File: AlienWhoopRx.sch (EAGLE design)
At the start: 16 parts, among them U1 XN297L, Y1 16MHZ

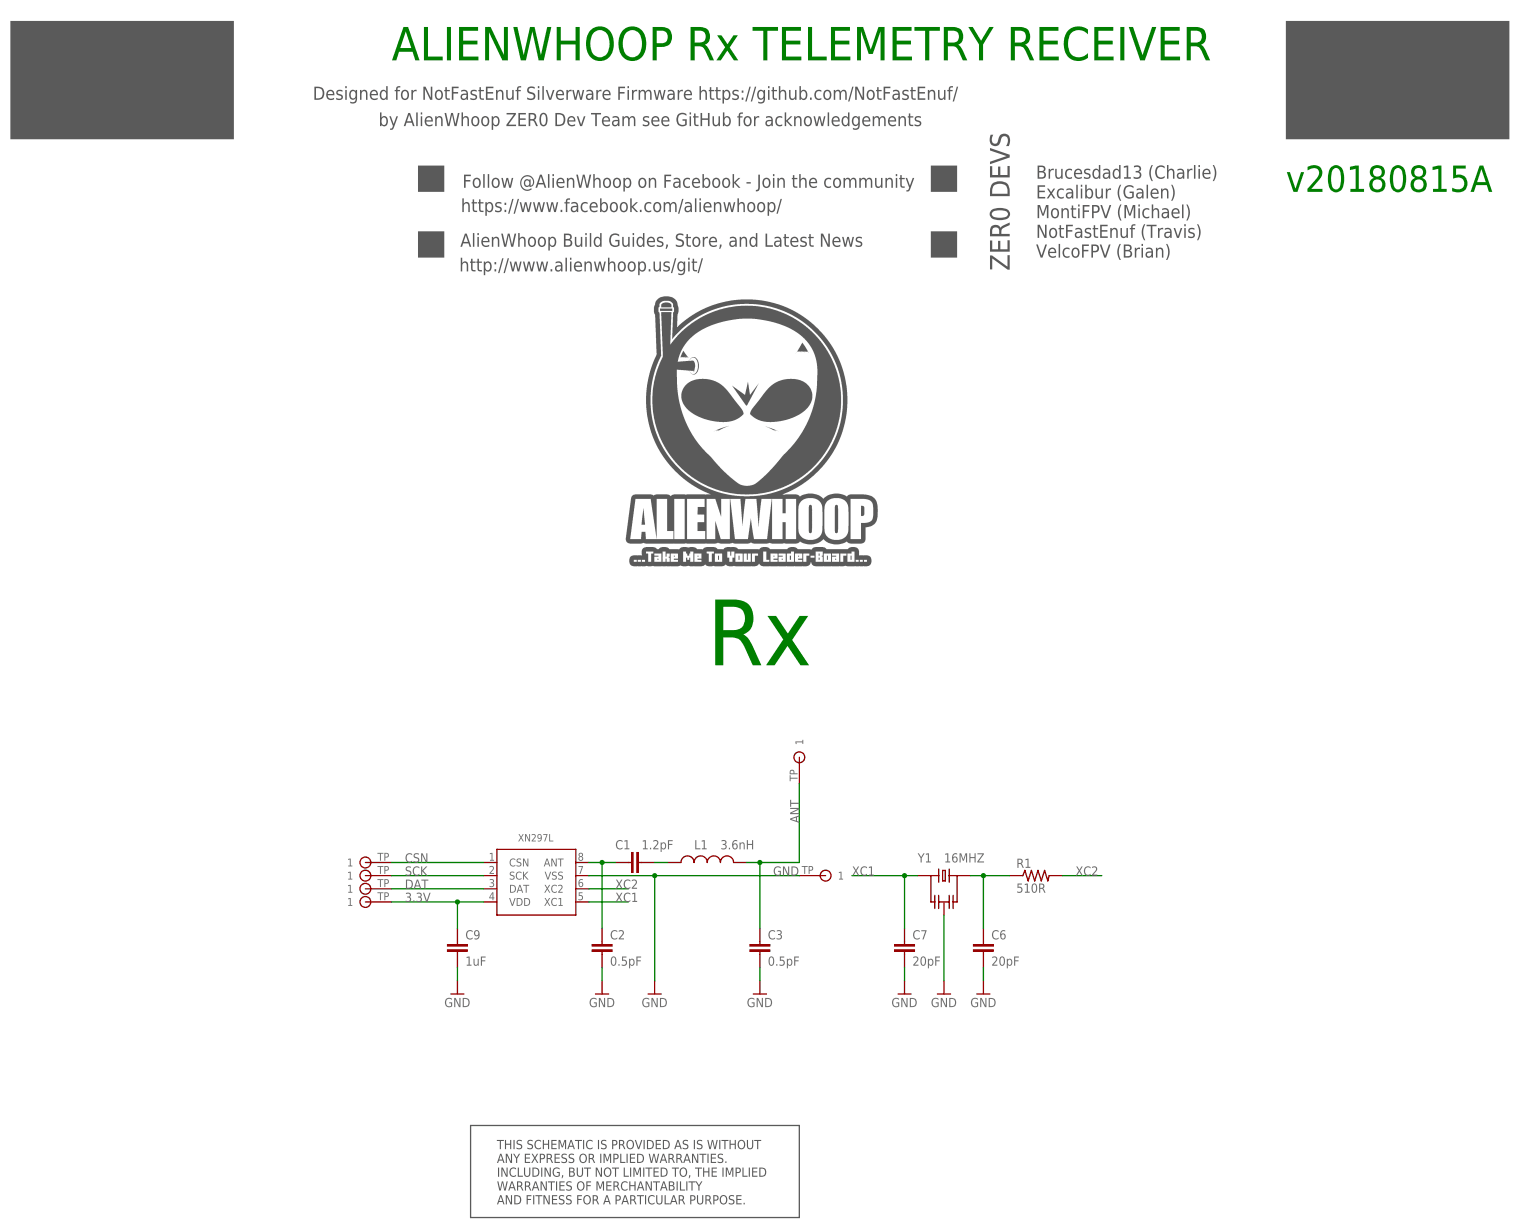
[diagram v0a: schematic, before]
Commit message: Shrunk overall dimensions. Second draft as ordered from OSH Park on 2018-09-06
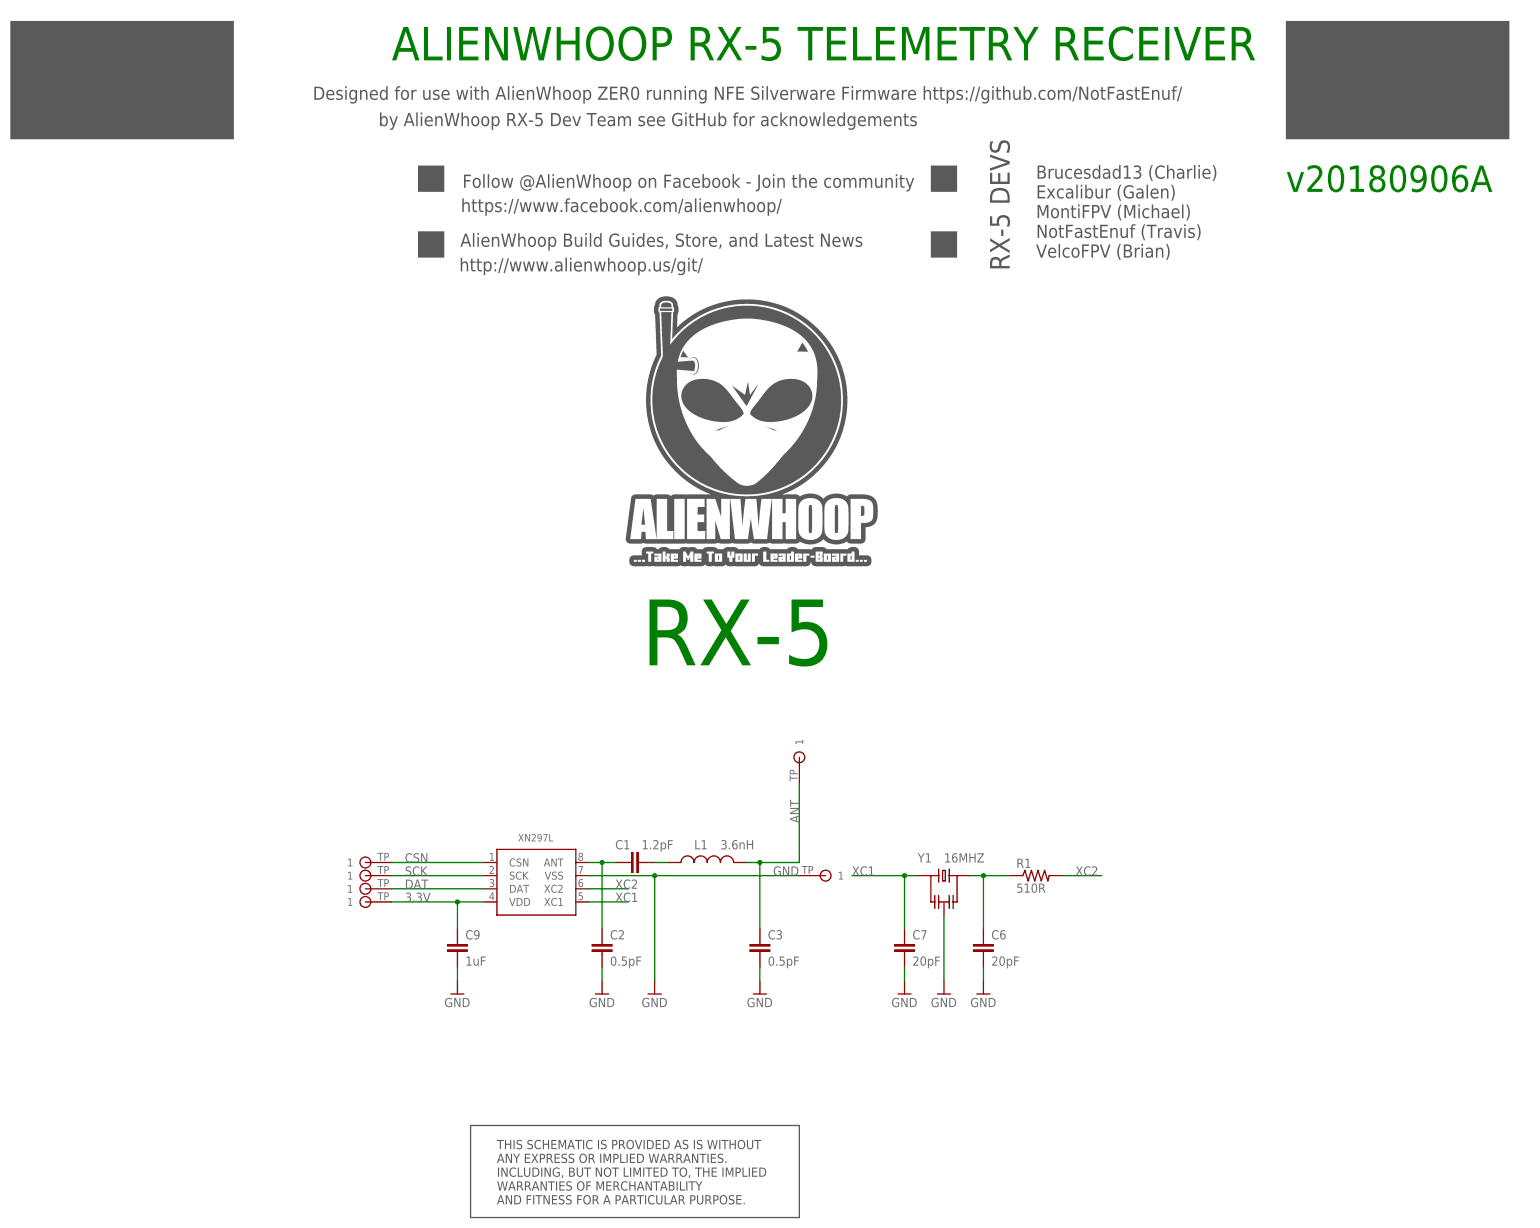
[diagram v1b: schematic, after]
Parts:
- C1: PARTNO (none) -> 0402YA1R2CAT2A
- C2, C3: PARTNO (none) -> VJ0402A0R5BXJCW1BC
- C6, C7: PARTNO (none) -> GJM1555C1H200FB01D
- C9: PARTNO (none) -> GRM155C71A105KE11D
- L1: PARTNO (none) -> MHQ1005P3N6ST000
- R1: PARTNO (none) -> CR0402-FX-5100GLF
- U1: PARTNO (none) -> XN297LBW
- Y1: PARTNO (none) -> ECS-160-20-33-CKM-TR
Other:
- note added: "ALIENWHOOP RX-5 TELEMETRY RECEIVER"
- note added: "Designed for use with AlienWhoop ZER0 running NFE Silverware Firmware https://github.com/NotFastEnuf/"
- note added: "RX-5"
- note added: "RX-5 DEVS"
- note added: "by AlienWhoop RX-5 Dev Team see GitHub for acknowledgements"
- note added: "v20180906A"
- note removed: "ALIENWHOOP Rx TELEMETRY RECEIVER"
- note removed: "Designed for NotFastEnuf Silverware Firmware https://github.com/NotFastEnuf/"
- note removed: "Rx"
- note removed: "ZER0 DEVS"
- note removed: "by AlienWhoop ZER0 Dev Team see GitHub for acknowledgements"
- note removed: "v20180815A"
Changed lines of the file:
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@@
 <part name="FRAME1" library="alienflight" deviceset="FRAME2" device=""/>
 <part name="SPI_CS" library="AlienWhoop" deviceset="TESTPAD" device=""/>
-<part name="U1" library="AlienWhoop" deviceset="XN297L" device=""/>
+<part name="U1" library="AlienWhoop" deviceset="XN297L" device="">
+<attribute name="PARTNO" value="XN297LBW"/>
+</part>
 <part name="U$6" library="AlienWhoop" deviceset="TESTPAD" device=""/>
 <part name="GND1" library="alienflight" deviceset="GND" device=""/>
-<part name="C9" library="Perfect_0402" deviceset="CAP_0402" device="" value="1uF"/>
+<part name="C9" library="Perfect_0402" deviceset="CAP_0402" device="" value="1uF">
+<attribute name="PARTNO" value="GRM155C71A105KE11D"/>
+</part>
 <part name="GND2" library="alienflight" deviceset="GND" device=""/>
-<part name="L1" library="alienflight" deviceset="MHQ1005P" device="3.6NH" value="3.6nH"/>
-<part name="C2" library="Perfect_0402" deviceset="CAP_0402" device="" value="0.5pF"/>
+<part name="L1" library="alienflight" deviceset="MHQ1005P" device="3.6NH" value="3.6nH">
+<attribute name="PARTNO" value="MHQ1005P3N6ST000"/>
+</part>
+<part name="C2" library="Perfect_0402" deviceset="CAP_0402" device="" value="0.5pF">
+<attribute name="PARTNO" value="VJ0402A0R5BXJCW1BC"/>
+</part>
 <part name="GND3" library="alienflight" deviceset="GND" device=""/>
-<part name="C3" library="Perfect_0402" deviceset="CAP_0402" device="" value="0.5pF"/>
+<part name="C3" library="Perfect_0402" deviceset="CAP_0402" device="" value="0.5pF">
+<attribute name="PARTNO" value="VJ0402A0R5BXJCW1BC"/>
+</part>
 <part name="GND4" library="alienflight" deviceset="GND" device=""/>
-<part name="C7" library="Perfect_0402" deviceset="CAP_0402" device="" value="20pF"/>
-<part name="C6" library="Perfect_0402" deviceset="CAP_0402" device="" value="20pF"/>
+<part name="C7" library="Perfect_0402" deviceset="CAP_0402" device="" value="20pF">
+<attribute name="PARTNO" value="GJM1555C1H200FB01D"/>
+</part>
+<part name="C6" library="Perfect_0402" deviceset="CAP_0402" device="" value="20pF">
+<attribute name="PARTNO" value="GJM1555C1H200FB01D"/>
+</part>
 <part name="GND6" library="alienflight" deviceset="GND" device=""/>
 <part name="GND7" library="alienflight" deviceset="GND" device=""/>
-<part name="R1" library="Perfect_0402" deviceset="RES_0402" device="" value="510R"/>
-<part name="Y1" library="AlienWhoop" deviceset="ECS-160-20-33-CKM-TR" device="16MHZ" value="16MHZ"/>
+<part name="R1" library="Perfect_0402" deviceset="RES_0402" device="" value="510R">
+<attribute name="PARTNO" value="CR0402-FX-5100GLF"/>
+</part>
+<part name="Y1" library="AlienWhoop" deviceset="ECS-160-20-33-CKM-TR" device="16MHZ" value="16MHZ">
+<attribute name="PARTNO" value="ECS-160-20-33-CKM-TR"/>
+</part>
 <part name="GND5" library="alienflight" deviceset="GND" device=""/>
-<part name="C1" library="Perfect_0402" deviceset="CAP_0402" device="" value="1.2pF"/>
+<part name="C1" library="Perfect_0402" deviceset="CAP_0402" device="" value="1.2pF">
+<attribute name="PARTNO" value="0402YA1R2CAT2A"/>
+</part>
 </parts>
 <sheets>
@@
 <rectangle x1="133.68655" y1="185.48985" x2="134.94385" y2="185.52795" layer="97"/>
 <rectangle x1="133.91515" y1="185.52795" x2="134.75335" y2="185.56605" layer="97"/>
-<text x="66.04" y="223.52" size="2.54" layer="97">Designed for NotFastEnuf Silverware Firmware https://github.com/NotFastEnuf/</text>
+<text x="66.04" y="223.52" size="2.54" layer="97">Designed for use with AlienWhoop ZER0 running NFE Silverware Firmware https://github.com/NotFastEnuf/</text>
 <text x="94.6404" y="201.8411" size="2.54" layer="97" font="vector">https://www.facebook.com/alienwhoop/</text>
 <text x="94.9452" y="206.5274" size="2.54" layer="97" font="vector" ratio="12">Follow @AlienWhoop on Facebook - Join the community</text>
@@
 <rectangle x1="185.42" y1="205.74" x2="190.5" y2="210.82" layer="97"/>
 <rectangle x1="185.42" y1="193.04" x2="190.5" y2="198.12" layer="97"/>
-<text x="78.74" y="218.44" size="2.54" layer="97">by AlienWhoop ZER0 Dev Team see GitHub for acknowledgements</text>
+<text x="78.74" y="218.44" size="2.54" layer="97">by AlienWhoop RX-5 Dev Team see GitHub for acknowledgements</text>
 <text x="94.3356" y="190.373" size="2.54" layer="97" font="vector">http://www.alienwhoop.us/git/</text>
 <text x="94.5261" y="195.1355" size="2.54" layer="97" font="vector" ratio="12">AlienWhoop Build Guides, Store, and Latest News</text>
 <rectangle x1="86.36" y1="193.04" x2="91.44" y2="198.12" layer="97"/>
-<text x="81.28" y="231.14" size="6.4516" layer="91" ratio="20">ALIENWHOOP Rx TELEMETRY RECEIVER</text>
+<text x="81.28" y="231.14" size="6.4516" layer="91" ratio="20">ALIENWHOOP RX-5 TELEMETRY RECEIVER</text>
 <rectangle x1="7.62" y1="215.9" x2="50.8" y2="238.76" layer="97"/>
 <rectangle x1="254" y1="215.9" x2="297.18" y2="238.76" layer="97"/>
-<text x="254" y="205.74" size="5.08" layer="91">v20180815A</text>
+<text x="254" y="205.74" size="5.08" layer="91">v20180906A</text>
 <text x="101.6" y="10.16" size="1.778" layer="97" ratio="10">THIS SCHEMATIC IS PROVIDED AS IS WITHOUT
 ANY EXPRESS OR IMPLIED WARRANTIES.
@@
 WARRANTIES OF MERCHANTABILITY
 AND FITNESS FOR A PARTICULAR PURPOSE.</text>
-<text x="142.24" y="114.3" size="12.7" layer="91" ratio="20">Rx</text>
+<text x="129.54" y="114.3" size="12.7" layer="91" ratio="20">RX-5</text>
 <wire x1="96.52" y1="25.4" x2="160.02" y2="25.4" width="0.1524" layer="97"/>
 <wire x1="160.02" y1="25.4" x2="160.02" y2="7.62" width="0.1524" layer="97"/>
@@
 NotFastEnuf (Travis)
 VelcoFPV (Brian)</text>
-<text x="200.66" y="190.5" size="3.81" layer="97" ratio="20" rot="R90">ZER0 DEVS</text>
+<text x="200.66" y="190.5" size="3.81" layer="97" ratio="20" rot="R90">RX-5 DEVS</text>
 </plain>
 <instances>
@@
 <instance part="FRAME1" gate="G$3" x="267.462" y="23.368"/>
 <instance part="SPI_CS" gate="G$1" x="76.2" y="76.2" rot="R180"/>
-<instance part="U1" gate="G$1" x="109.22" y="68.58"/>
+<instance part="U1" gate="G$1" x="109.22" y="68.58">
+<attribute name="PARTNO" x="109.22" y="68.58" size="1.778" layer="96" display="off"/>
+</instance>
 <instance part="U$6" gate="G$1" x="160.02" y="96.52" rot="R90"/>
 <instance part="GND1" gate="1" x="132.08" y="50.8"/>
-<instance part="C9" gate="G$1" x="93.98" y="55.88"/>
+<instance part="C9" gate="G$1" x="93.98" y="55.88">
+<attribute name="PARTNO" x="93.98" y="55.88" size="1.778" layer="96" display="off"/>
+</instance>
 <instance part="GND2" gate="1" x="93.98" y="50.8"/>
 <instance part="L1" gate="G$1" x="142.24" y="76.2" smashed="yes">
 <attribute name="NAME" x="139.7" y="78.74" size="1.778" layer="95" font="vector"/>
 <attribute name="VALUE" x="144.78" y="78.74" size="1.778" layer="96" font="vector"/>
+<attribute name="PARTNO" x="142.24" y="76.2" size="1.778" layer="96" display="off"/>
+</instance>
+<instance part="C2" gate="G$1" x="121.92" y="55.88">
+<attribute name="PARTNO" x="121.92" y="55.88" size="1.778" layer="96" display="off"/>
 </instance>
-<instance part="C2" gate="G$1" x="121.92" y="55.88"/>
 <instance part="GND3" gate="1" x="121.92" y="50.8"/>
-<instance part="C3" gate="G$1" x="152.4" y="55.88"/>
+<instance part="C3" gate="G$1" x="152.4" y="55.88">
+<attribute name="PARTNO" x="152.4" y="55.88" size="1.778" layer="96" display="off"/>
+</instance>
 <instance part="GND4" gate="1" x="152.4" y="50.8"/>
-<instance part="C7" gate="G$1" x="180.34" y="55.88"/>
-<instance part="C6" gate="G$1" x="195.58" y="55.88"/>
+<instance part="C7" gate="G$1" x="180.34" y="55.88">
+<attribute name="PARTNO" x="180.34" y="55.88" size="1.778" layer="96" display="off"/>
+</instance>
+<instance part="C6" gate="G$1" x="195.58" y="55.88">
+<attribute name="PARTNO" x="195.58" y="55.88" size="1.778" layer="96" display="off"/>
+</instance>
 <instance part="GND6" gate="1" x="180.34" y="50.8"/>
 <instance part="GND7" gate="1" x="195.58" y="50.8"/>
-<instance part="R1" gate="G$1" x="200.66" y="73.66"/>
+<instance part="R1" gate="G$1" x="200.66" y="73.66">
+<attribute name="PARTNO" x="200.66" y="73.66" size="1.778" layer="96" display="off"/>
+</instance>
 <instance part="Y1" gate="G$1" x="187.96" y="71.12" smashed="yes">
 <attribute name="NAME" x="182.88" y="76.2" size="1.778" layer="95"/>
 <attribute name="VALUE" x="187.96" y="76.2" size="1.778" layer="96"/>
+<attribute name="PARTNO" x="187.96" y="71.12" size="1.778" layer="96" display="off"/>
 </instance>
 <instance part="GND5" gate="1" x="187.96" y="50.8"/>
@@
 <attribute name="NAME" x="124.46" y="78.74" size="1.778" layer="95"/>
 <attribute name="VALUE" x="129.54" y="78.74" size="1.778" layer="96"/>
+<attribute name="PARTNO" x="132.08" y="76.2" size="1.778" layer="96" display="off"/>
 </instance>
 </instances>
